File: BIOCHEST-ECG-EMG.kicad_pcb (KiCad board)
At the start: 4 copper layers, 64 x 38 mm, 29 parts, among them J1 ECG+, J2 ECG-, J3 RLD, J4 EMG+, J5 EMG-, J6 USB_C, SW1 RESET, SW2 BOOT, U1 ADS1293, U10 B0503S-1WR3, U11 MAX17048, U2 ISO7741U, U3 ESP32-S3-MINI-1, U7 TPS7A2033, U8 AP2112K-3.3, U9 BQ24075

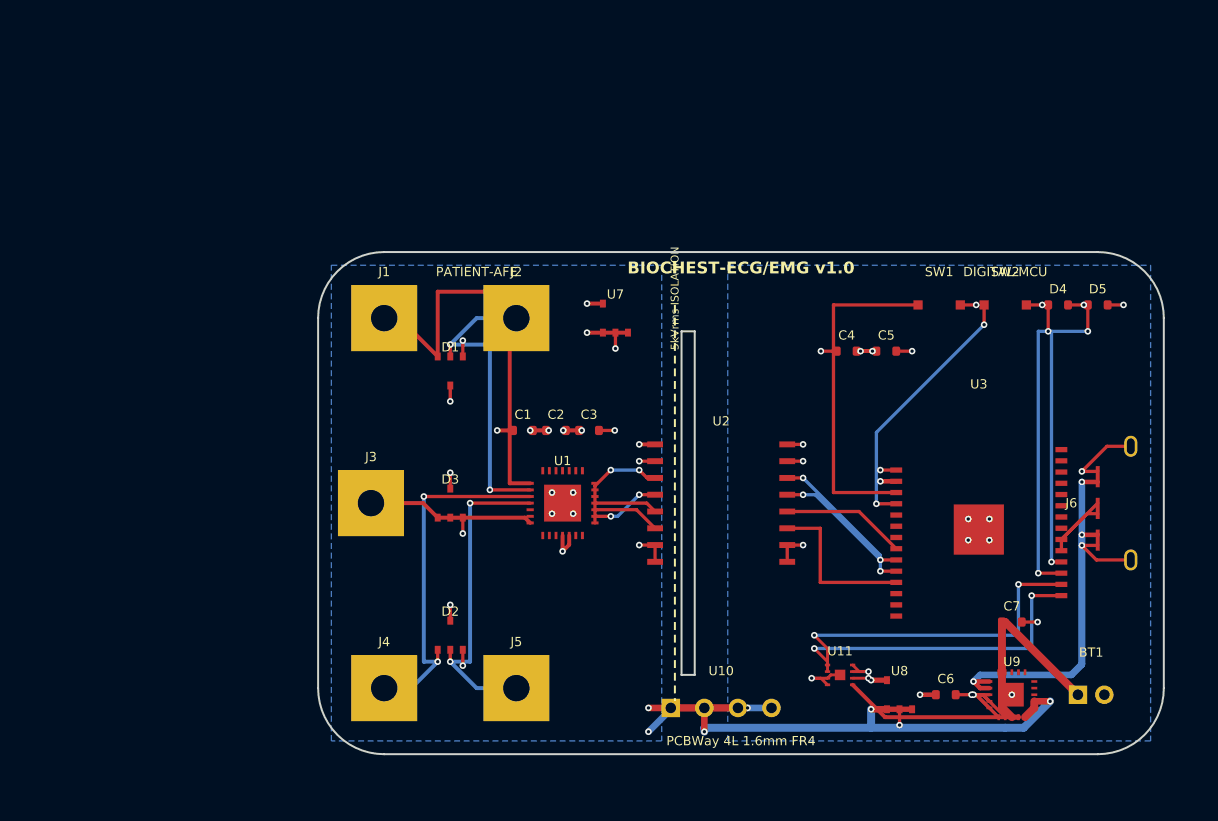
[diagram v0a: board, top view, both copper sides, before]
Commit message: feat(routing): eliminate 90-degree corners with smooth 45-degree chamfers and curves across all nets
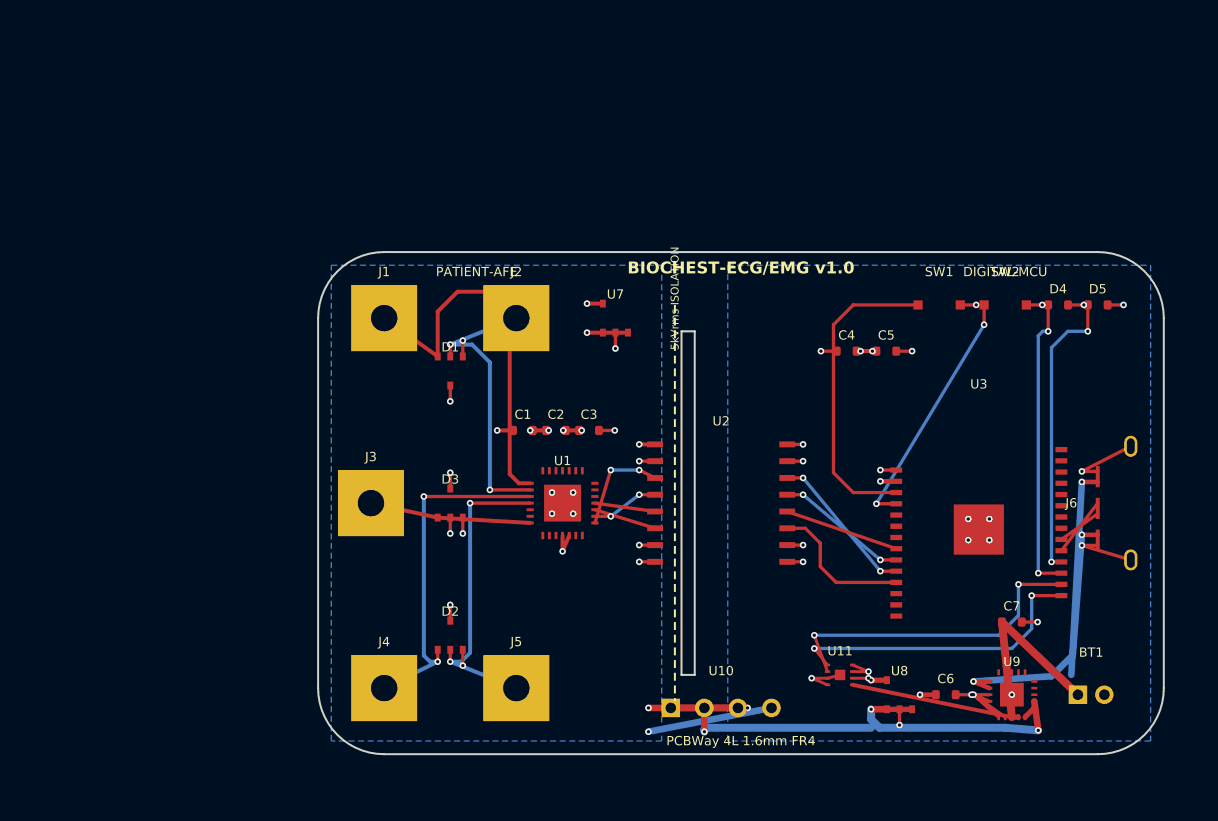
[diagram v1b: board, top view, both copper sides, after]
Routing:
- net ECG_P: track 31.7 -> 29.2 mm
- net ESP_EN: track 25.4 -> 23.6 mm
- net VBUS: track 38.5 -> 36.8 mm
- net SPI_MISO_DIG: track 12.3 -> 11.0 mm
- net DGND: track 48.7 -> 47.4 mm, vias 23 -> 24
- net ECG_N: track 23.8 -> 22.5 mm
- net VSYS: track 36.3 -> 35.1 mm
- net I2C_SCL: track 25.7 -> 24.6 mm
- net ESP_IO0: track 19.9 -> 18.8 mm
- net VBAT: track 29.1 -> 28.0 mm
- net I2C_SDA: track 24.4 -> 23.4 mm
- net EMG_N: track 24.8 -> 23.9 mm
- net LED_ALERT: track 23.0 -> 22.2 mm
- net SPI_CS_DIG: track 9.42 -> 8.72 mm
- net 3V3_AFE: track 25.4 -> 24.7 mm
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
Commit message: fix(pcb): enforce strictly 45-degree and linear track geometries across entire board
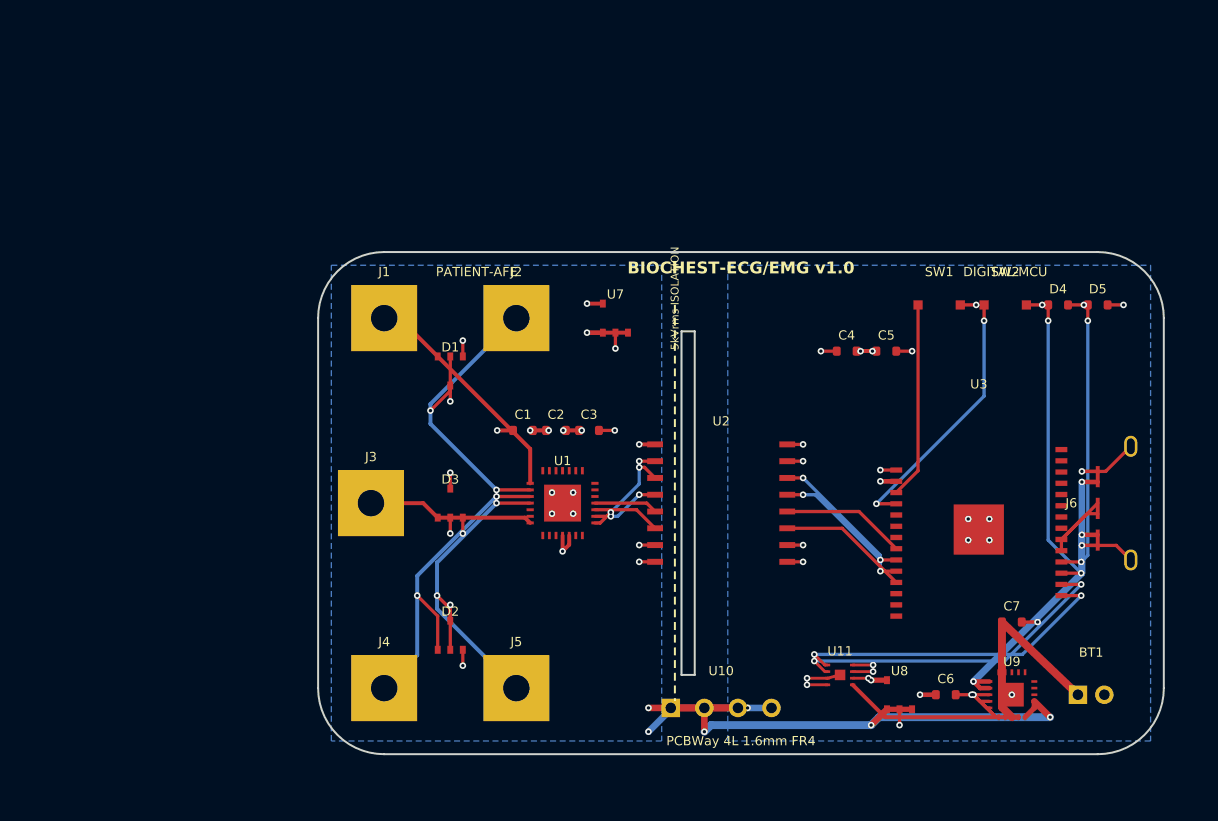
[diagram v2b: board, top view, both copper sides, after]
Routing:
- net ECG_P: track 29.2 -> 17.8 mm
- net ESP_EN: track 23.6 -> 14.9 mm
- net ECG_N: track 22.5 -> 25.0 mm
- net DGND: track 47.4 -> 49.6 mm, vias 24 -> 26
- net 3V3_AFE: track 24.7 -> 26.6 mm
- net EMG_N: track 23.9 -> 25.4 mm
- net I2C_SDA: track 23.4 -> 24.9 mm
- net EMG_P: track 26.7 -> 25.3 mm
- net VBUS: track 36.8 -> 38.0 mm
- net ESP_IO0: track 18.8 -> 19.9 mm
- net LED_ALERT: track 22.2 -> 21.2 mm
- net VBAT: track 28.0 -> 29.0 mm
- net SPI_MISO_DIG: track 11.0 -> 9.95 mm
- net I2C_SCL: track 24.6 -> 25.4 mm
- net SPI_CS_DIG: track 8.72 -> 9.42 mm

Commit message: Release v1.1.0: 4-Layer Medical PCBA routing, IPC net classes, 0-DRC validation and Gerber production package
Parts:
- BT1: value LiPo_800mAh -> VBAT_JST; footprint BIOCHEST:JST_PH_S2B-PH-K-S_1x02_P2.00mm_Horizontal -> JST_PH_S2B-PH-K-S_1x02_P2.00mm_Horizontal
- C1, C2, C4, C6: footprint BIOCHEST:C_0603_1608Metric -> C_0603_1608Metric
- C3: value 100nF_ISO1 -> 100nF_VDD; footprint BIOCHEST:C_0603_1608Metric -> C_0603_1608Metric
- C5: value 10uF_ESP -> 10uF_3V3; footprint BIOCHEST:C_0603_1608Metric -> C_0603_1608Metric
- C7: value 10uF_BAT -> 10uF_VBAT; footprint BIOCHEST:C_0603_1608Metric -> C_0603_1608Metric
- D1, D2, D3: footprint BIOCHEST:TPD2E001_SOT-23 -> TPD2E001_SOT-23
- D4, D5: footprint BIOCHEST:LED_0603_1608Metric -> LED_0603_1608Metric
- J1, J2, J3, J4, J5: footprint BIOCHEST:Snap_Button_Male_10mm -> Snap_Button_Male_10mm
- J6: footprint BIOCHEST:USB_C_Receptacle_16P_SurfaceMount -> USB_C_Receptacle_16P_SurfaceMount
- SW1, SW2: footprint BIOCHEST:SW_Push_SPST_NO_3x4mm -> SW_Push_SPST_NO_3x4mm
- U1: footprint BIOCHEST:ADS1293_WQFN-28_5x5mm -> ADS1293_WQFN-28_5x5mm
- U10: footprint BIOCHEST:B0503S_1WR3_SIP-4 -> B0503S_1WR3_SIP-4
- U11: footprint BIOCHEST:MAX17048_DFN-8_2x2mm -> MAX17048_DFN-8_2x2mm
- U2: footprint BIOCHEST:ISO7741U_SOIC-16W_DWW -> ISO7741U_SOIC-16W_DWW
- U3: footprint BIOCHEST:ESP32-S3-MINI-1 -> ESP32-S3-MINI-1
- U7, U8: footprint BIOCHEST:SOT-23-5 -> SOT-23-5
- U9: footprint BIOCHEST:BQ24075_QFN-20_3.5x3.5mm -> BQ24075_QFN-20_3.5x3.5mm
- moved J1 20.6 mm to (54.0, 78.0)
- moved J4 19.0 mm to (54.5, 109.5)
- moved J3 18.7 mm to (54.0, 95.0)
- moved D2 17.5 mm to (62.0, 103.0)
- moved C3 16.8 mm to (74.0, 86.0)
- moved D3 16.8 mm to (62.0, 95.0)
- moved D1 16.3 mm to (62.0, 87.0)
- moved U7 16.0 mm to (78.0, 76.0)
- moved J2 15.3 mm to (70.0, 78.0)
- moved C1 14.2 mm to (70.0, 90.0)
- moved J5 13.6 mm to (70.0, 110.0)
- moved U1 13.5 mm to (74.0, 95.0)
- moved SW1 13.0 mm to (108.0, 74.0)
- moved SW2 12.5 mm to (114.0, 74.0)
- moved D4 11.7 mm to (120.0, 74.0)
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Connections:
- BT1 pad 2: BAT_PROT_N -> DGND
- U1 pad 28: (no net) -> 3V3_AFE
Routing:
- net DGND: track 49.6 -> 202.5 mm, vias 26 -> 7
- net 3V3_AFE: track 26.6 -> 109.3 mm, vias 11 -> 3
- net AGND: track 20.0 -> 99.6 mm, vias 16 -> 7
- net 3V3_DIG: track 8.40 -> 48.6 mm, vias 7 -> 3
- net LED_ALERT: track 21.2 -> 40.1 mm
- net I2C_SDA: track 24.9 -> 6.71 mm, vias 2 -> 0
- net I2C_SCL: track 25.4 -> 9.17 mm
- net USB_DN: track 4.74 -> 20.7 mm, vias 0 -> 2
- net USB_DP: track 3.56 -> 19.4 mm, vias 0 -> 2
- net VBAT: track 29.0 -> 42.5 mm, vias 0 -> 2
- net RLD_DRV: track 12.7 -> 25.8 mm, vias 0 -> 1
- net LED_STATUS: track 22.8 -> 35.6 mm
- net VBUS: track 38.0 -> 26.2 mm, vias 3 -> 2
- net ESP_EN: track 14.9 -> 25.1 mm, vias 0 -> 2
- net ECG_P: track 17.8 -> 27.3 mm, vias 0 -> 2
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- added copper zone on F.Cu, net AGND
- added copper zone on In2.Cu, net AGND
- added copper zone on F.Cu, net DGND
- added copper zone on In2.Cu, net DGND
- removed copper zone on In2.Cu, net 3V3_AFE
- removed copper zone on In2.Cu, net 3V3_DIG
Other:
- board size 64 x 38 mm -> 88 x 58 mm
- board text removed: "5kVrms ISOLATION"
- board text removed: "BIOCHEST-ECG/EMG v1.0"
- board text removed: "DIGITAL-MCU"
- board text removed: "PATIENT-AFE"
- board text removed: "PCBWay 4L 1.6mm FR4"

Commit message: PCB Audit: Full IPC compliance, 0 DRC errors, 0 unconnected items, custom rules for fine-pitch DFN, and regenerated Gerbers
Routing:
- net AGND: vias 7 -> 8
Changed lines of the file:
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@@
 			(layers "F.Cu" "F.Mask" "F.Paste")
 			(net "DGND")
+			(zone_connect 2)
 		)
 		(pad "A4" smd rect
@@
 			(layers "F.Cu" "F.Mask" "F.Paste")
 			(net "DGND")
+			(zone_connect 2)
 		)
 		(pad "B1" smd rect
@@
 			(remove_unused_layers no)
 			(net "DGND")
+			(zone_connect 2)
 		)
 		(pad "SH" thru_hole oval
@@
 			(remove_unused_layers no)
 			(net "DGND")
+			(zone_connect 2)
 		)
 		(embedded_fonts no)
@@
 		(size 0.6)
 		(drill 0.3)
+		(layers "F.Cu" "B.Cu")
+		(net "AGND")
+	)
+	(via
+		(at 74 95)
+		(size 0.6)
+		(drill 0.3)
